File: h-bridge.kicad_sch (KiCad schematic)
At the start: 10 parts, among them U5 DRV8874, U6 INA241A3IDDF

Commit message: schem: add missing footprints
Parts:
- R3: footprint (none) -> Resistor_SMD:R_0805_2012Metric
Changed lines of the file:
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@@
 			)
 		)
-		(property "Footprint" ""
+		(property "Footprint" "Resistor_SMD:R_0805_2012Metric"
 			(at 168.91 90.678 90)
 			(hide yes)

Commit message: schem: add ordering info to BOM
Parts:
- R3: Basic (none) -> X; JLCPCB Part # (none) -> C22450688; Manufacturer (none) -> Milliohm; Manufacturer Part Number (none) -> HoYLR0805-1/2W-10mR-1%
- U5: Basic (none) -> X; JLCPCB Part # (none) -> C1855818; Manufacturer (none) -> Texas Instruments; Manufacturer Part Number (none) -> DRV8874PWPR
- U6: Basic (none) -> X; JLCPCB Part # (none) -> C6051860; Manufacturer (none) -> Texas Instruments; Manufacturer Part Number (none) -> INA241A3IDDFR

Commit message: schem: add title
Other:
- company: (none) -> Rémi Ait-Younes
- title: (none) -> Stepper FOC CAN 1
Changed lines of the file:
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@@
 	(generator_version "10.0")
 	(paper "A4")
+	(title_block
+		(title "Stepper FOC CAN 1")
+		(date "2026-04-11")
+		(rev "01")
+		(company "Rémi Ait-Younes")
+	)
 	(text "Gain: 50V/V\nRange: ±3.35A"
 		(exclude_from_sim no)

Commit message: schem: reannotate
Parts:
- renumbered C26 to C29, C25 to C30, R6 to R10, R3 to R11, TP5 to TP2, U5 to U6, U6 to U7
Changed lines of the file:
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@@
 		(in_pos_files yes)
 		(dnp no)
-		(property "Reference" "#PWR035"
+		(property "Reference" "#PWR049"
 			(at 129.54 119.38 0)
 			(hide yes)
@@
 			(project "stepper-foc-can-1"
 				(path "/7e511d2f-8abe-4907-a647-133ba6c8a8df/0e6f64a8-6e8e-4ac8-9891-7840f5dbe0f5"
-					(reference "#PWR035")
+					(reference "#PWR049")
 					(unit 1)
 				)
 				(path "/7e511d2f-8abe-4907-a647-133ba6c8a8df/8e42ab5e-b2ac-4617-9b8b-7bb81c6c35e1"
-					(reference "#PWR054")
+					(reference "#PWR059")
 					(unit 1)
 				)
@@
 		(in_pos_files yes)
 		(dnp no)
-		(property "Reference" "#PWR045"
+		(property "Reference" "#PWR048"
 			(at 129.54 83.82 0)
 			(hide yes)
@@
 			(project "stepper-foc-can-1"
 				(path "/7e511d2f-8abe-4907-a647-133ba6c8a8df/0e6f64a8-6e8e-4ac8-9891-7840f5dbe0f5"
-					(reference "#PWR045")
+					(reference "#PWR048")
 					(unit 1)
 				)
 				(path "/7e511d2f-8abe-4907-a647-133ba6c8a8df/8e42ab5e-b2ac-4617-9b8b-7bb81c6c35e1"
-					(reference "#PWR053")
+					(reference "#PWR058")
 					(unit 1)
 				)
@@
 		(in_pos_files yes)
 		(dnp no)
-		(property "Reference" "U6"
+		(property "Reference" "U7"
 			(at 161.798 96.266 90)
 			(show_name no)
@@
 			(project "stepper-foc-can-1"
 				(path "/7e511d2f-8abe-4907-a647-133ba6c8a8df/0e6f64a8-6e8e-4ac8-9891-7840f5dbe0f5"
-					(reference "U6")
+					(reference "U7")
 					(unit 1)
 				)
 				(path "/7e511d2f-8abe-4907-a647-133ba6c8a8df/8e42ab5e-b2ac-4617-9b8b-7bb81c6c35e1"
-					(reference "U8")
+					(reference "U9")
 					(unit 1)
 				)
@@
 				)
 				(path "/7e511d2f-8abe-4907-a647-133ba6c8a8df/8e42ab5e-b2ac-4617-9b8b-7bb81c6c35e1"
-					(reference "#PWR051")
+					(reference "#PWR056")
 					(unit 1)
 				)
@@
 		(in_pos_files yes)
 		(dnp no)
-		(property "Reference" "TP5"
+		(property "Reference" "TP2"
 			(at 167.386 115.062 0)
 			(show_name no)
@@
 			(project "stepper-foc-can-1"
 				(path "/7e511d2f-8abe-4907-a647-133ba6c8a8df/0e6f64a8-6e8e-4ac8-9891-7840f5dbe0f5"
-					(reference "TP5")
+					(reference "TP2")
 					(unit 1)
 				)
 				(path "/7e511d2f-8abe-4907-a647-133ba6c8a8df/8e42ab5e-b2ac-4617-9b8b-7bb81c6c35e1"
-					(reference "TP6")
+					(reference "TP3")
 					(unit 1)
 				)
@@
 		(in_pos_files yes)
 		(dnp no)
-		(property "Reference" "#PWR050"
+		(property "Reference" "#PWR052"
 			(at 156.21 111.76 0)
 			(hide yes)
@@
 			(project "stepper-foc-can-1"
 				(path "/7e511d2f-8abe-4907-a647-133ba6c8a8df/0e6f64a8-6e8e-4ac8-9891-7840f5dbe0f5"
-					(reference "#PWR050")
+					(reference "#PWR052")
 					(unit 1)
 				)
 				(path "/7e511d2f-8abe-4907-a647-133ba6c8a8df/8e42ab5e-b2ac-4617-9b8b-7bb81c6c35e1"
-					(reference "#PWR057")
+					(reference "#PWR062")
 					(unit 1)
 				)
@@
 		(in_pos_files yes)
 		(dnp no)
-		(property "Reference" "C26"
+		(property "Reference" "C29"
 			(at 150.876 66.04 0)
 			(show_name no)
@@
 			(project "stepper-foc-can-1"
 				(path "/7e511d2f-8abe-4907-a647-133ba6c8a8df/0e6f64a8-6e8e-4ac8-9891-7840f5dbe0f5"
-					(reference "C26")
+					(reference "C29")
 					(unit 1)
 				)
@@
 		(in_pos_files yes)
 		(dnp no)
-		(property "Reference" "C25"
+		(property "Reference" "C30"
 			(at 159.258 76.2 0)
 			(show_name no)
@@
 			(project "stepper-foc-can-1"
 				(path "/7e511d2f-8abe-4907-a647-133ba6c8a8df/0e6f64a8-6e8e-4ac8-9891-7840f5dbe0f5"
-					(reference "C25")
+					(reference "C30")
 					(unit 1)
 				)
@@
 		(in_pos_files yes)
 		(dnp no)
-		(property "Reference" "#PWR043"
+		(property "Reference" "#PWR053"
 			(at 157.48 73.66 0)
 			(hide yes)
@@
 			(project "stepper-foc-can-1"
 				(path "/7e511d2f-8abe-4907-a647-133ba6c8a8df/0e6f64a8-6e8e-4ac8-9891-7840f5dbe0f5"
-					(reference "#PWR043")
+					(reference "#PWR053")
 					(unit 1)
 				)
 				(path "/7e511d2f-8abe-4907-a647-133ba6c8a8df/8e42ab5e-b2ac-4617-9b8b-7bb81c6c35e1"
-					(reference "#PWR058")
+					(reference "#PWR063")
 					(unit 1)
 				)
@@
 		(in_pos_files yes)
 		(dnp no)
-		(property "Reference" "#PWR048"
+		(property "Reference" "#PWR054"
 			(at 177.8 102.87 0)
 			(hide yes)
@@
 			(project "stepper-foc-can-1"
 				(path "/7e511d2f-8abe-4907-a647-133ba6c8a8df/0e6f64a8-6e8e-4ac8-9891-7840f5dbe0f5"
-					(reference "#PWR048")
+					(reference "#PWR054")
 					(unit 1)
 				)
 				(path "/7e511d2f-8abe-4907-a647-133ba6c8a8df/8e42ab5e-b2ac-4617-9b8b-7bb81c6c35e1"
-					(reference "#PWR059")
+					(reference "#PWR064")
 					(unit 1)
 				)
@@
 		(in_pos_files yes)
 		(dnp no)
-		(property "Reference" "#PWR044"
+		(property "Reference" "#PWR047"
 			(at 115.57 114.3 0)
 			(hide yes)
@@
 			(project "stepper-foc-can-1"
 				(path "/7e511d2f-8abe-4907-a647-133ba6c8a8df/0e6f64a8-6e8e-4ac8-9891-7840f5dbe0f5"
-					(reference "#PWR044")
+					(reference "#PWR047")
 					(unit 1)
 				)
 				(path "/7e511d2f-8abe-4907-a647-133ba6c8a8df/8e42ab5e-b2ac-4617-9b8b-7bb81c6c35e1"
-					(reference "#PWR052")
+					(reference "#PWR057")
 					(unit 1)
 				)
@@
 		(in_pos_files yes)
 		(dnp no)
-		(property "Reference" "R6"
+		(property "Reference" "R10"
 			(at 103.124 90.17 0)
 			(show_name no)
@@
 			(project "stepper-foc-can-1"
 				(path "/7e511d2f-8abe-4907-a647-133ba6c8a8df/0e6f64a8-6e8e-4ac8-9891-7840f5dbe0f5"
-					(reference "R6")
+					(reference "R10")
 					(unit 1)
 				)
 				(path "/7e511d2f-8abe-4907-a647-133ba6c8a8df/8e42ab5e-b2ac-4617-9b8b-7bb81c6c35e1"
-					(reference "R7")
+					(reference "R12")
 					(unit 1)
 				)
@@
 		(in_pos_files yes)
 		(dnp no)
-		(property "Reference" "#PWR036"
+		(property "Reference" "#PWR050"
 			(at 149.86 88.9 0)
 			(hide yes)
@@
 			(project "stepper-foc-can-1"
 				(path "/7e511d2f-8abe-4907-a647-133ba6c8a8df/0e6f64a8-6e8e-4ac8-9891-7840f5dbe0f5"
-					(reference "#PWR036")
+					(reference "#PWR050")
 					(unit 1)
 				)
 				(path "/7e511d2f-8abe-4907-a647-133ba6c8a8df/8e42ab5e-b2ac-4617-9b8b-7bb81c6c35e1"
-					(reference "#PWR055")
+					(reference "#PWR060")
 					(unit 1)
 				)
@@
 		(in_pos_files yes)
 		(dnp no)
-		(property "Reference" "#PWR047"
+		(property "Reference" "#PWR051"
 			(at 156.21 107.95 0)
 			(hide yes)
@@
 			(project "stepper-foc-can-1"
 				(path "/7e511d2f-8abe-4907-a647-133ba6c8a8df/0e6f64a8-6e8e-4ac8-9891-7840f5dbe0f5"
-					(reference "#PWR047")
+					(reference "#PWR051")
 					(unit 1)
 				)
 				(path "/7e511d2f-8abe-4907-a647-133ba6c8a8df/8e42ab5e-b2ac-4617-9b8b-7bb81c6c35e1"
-					(reference "#PWR056")
+					(reference "#PWR061")
 					(unit 1)
 				)
@@
 		(in_pos_files yes)
 		(dnp no)
-		(property "Reference" "R3"
+		(property "Reference" "R11"
 			(at 168.91 84.074 90)
 			(show_name no)
@@
 			(project "stepper-foc-can-1"
 				(path "/7e511d2f-8abe-4907-a647-133ba6c8a8df/0e6f64a8-6e8e-4ac8-9891-7840f5dbe0f5"
-					(reference "R3")
+					(reference "R11")
 					(unit 1)
 				)
 				(path "/7e511d2f-8abe-4907-a647-133ba6c8a8df/8e42ab5e-b2ac-4617-9b8b-7bb81c6c35e1"
-					(reference "R12")
+					(reference "R13")
 					(unit 1)
 				)
@@
 		(in_pos_files yes)
 		(dnp no)
-		(property "Reference" "#PWR049"
+		(property "Reference" "#PWR055"
 			(at 177.8 116.84 0)
 			(hide yes)
@@
 			(project "stepper-foc-can-1"
 				(path "/7e511d2f-8abe-4907-a647-133ba6c8a8df/0e6f64a8-6e8e-4ac8-9891-7840f5dbe0f5"
-					(reference "#PWR049")
+					(reference "#PWR055")
 					(unit 1)
 				)
 				(path "/7e511d2f-8abe-4907-a647-133ba6c8a8df/8e42ab5e-b2ac-4617-9b8b-7bb81c6c35e1"
-					(reference "#PWR060")
+					(reference "#PWR065")
 					(unit 1)
 				)
@@
 		(in_pos_files yes)
 		(dnp no)
-		(property "Reference" "U5"
+		(property "Reference" "U6"
 			(at 131.064 111.252 0)
 			(show_name no)
@@
 			(project "stepper-foc-can-1"
 				(path "/7e511d2f-8abe-4907-a647-133ba6c8a8df/0e6f64a8-6e8e-4ac8-9891-7840f5dbe0f5"
-					(reference "U5")
+					(reference "U6")
 					(unit 1)
 				)
 				(path "/7e511d2f-8abe-4907-a647-133ba6c8a8df/8e42ab5e-b2ac-4617-9b8b-7bb81c6c35e1"
-					(reference "U7")
-					(unit 1)
-				)
+					(reference "U8")
+					(unit 1)
+				)

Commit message: schem: update 22n capacitor PN
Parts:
- C28: footprint Capacitor_SMD:C_0603_1608Metric -> Capacitor_SMD:C_0402_1005Metric; JLCPCB Part # C21122 -> C1532; Manufacturer Samsung Electro-Mechanics -> FH (Guangdong Fenghua Advanced Tech); Manufacturer Part Number CL10B223KB8NNNC -> 0402B223K500NT
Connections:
- net GND: now also U6.17 (EPAD)
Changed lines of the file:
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@@
 			)
 		)
-		(property "Footprint" "Capacitor_SMD:C_0603_1608Metric"
+		(property "Footprint" "Capacitor_SMD:C_0402_1005Metric"
 			(at 151.13 100.6348 0)
 			(hide yes)
@@
 			)
 		)
-		(property "JLCPCB Part #" "C21122"
+		(property "JLCPCB Part #" "C1532"
 			(at 147.32 101.6 90)
 			(hide yes)
@@
 			)
 		)
-		(property "Manufacturer" "Samsung Electro-Mechanics "
+		(property "Manufacturer" "FH (Guangdong Fenghua Advanced Tech)"
 			(at 147.32 101.6 90)
 			(hide yes)
@@
 			)
 		)
-		(property "Manufacturer Part Number" "CL10B223KB8NNNC"
-			(at 147.32 101.6 90)
-			(hide yes)
-			(show_name no)
-			(do_not_autoplace no)
-			(effects
-				(font
-					(size 1.27 1.27)
-				)
-			)
-		)
-		(property "KLC_S3.3" ""
-			(at 147.32 101.6 90)
-			(hide yes)
-			(show_name no)
-			(do_not_autoplace no)
-			(effects
-				(font
-					(size 1.27 1.27)
-				)
-			)
-		)
-		(property "KLC_S4.1" ""
+		(property "Manufacturer Part Number" "0402B223K500NT"
 			(at 147.32 101.6 90)
 			(hide yes)
@@
 		(pin "5"
 		)
+		(pin "17"
+		)
 		(instances

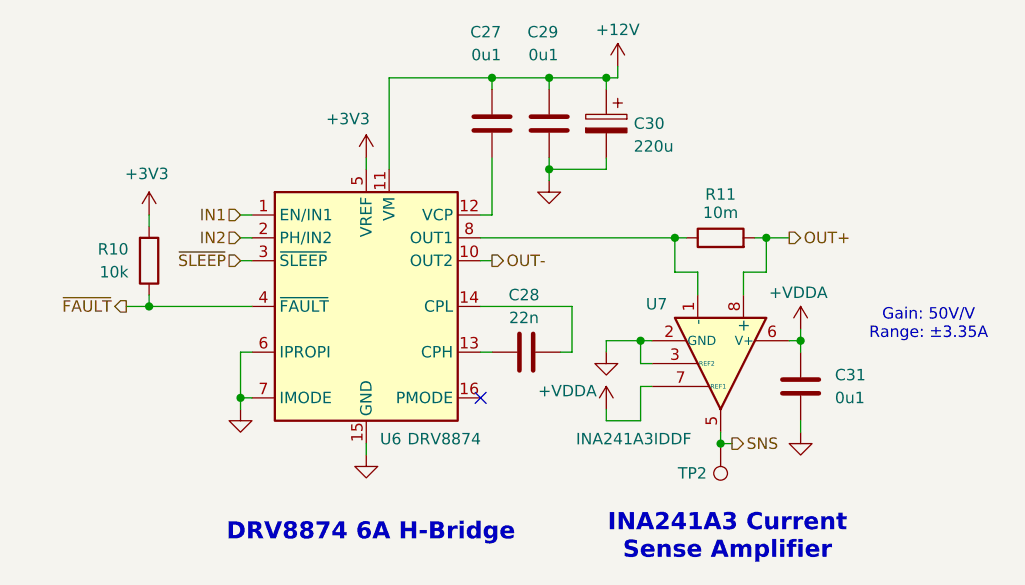
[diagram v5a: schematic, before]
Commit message: pcb: add drvs placement
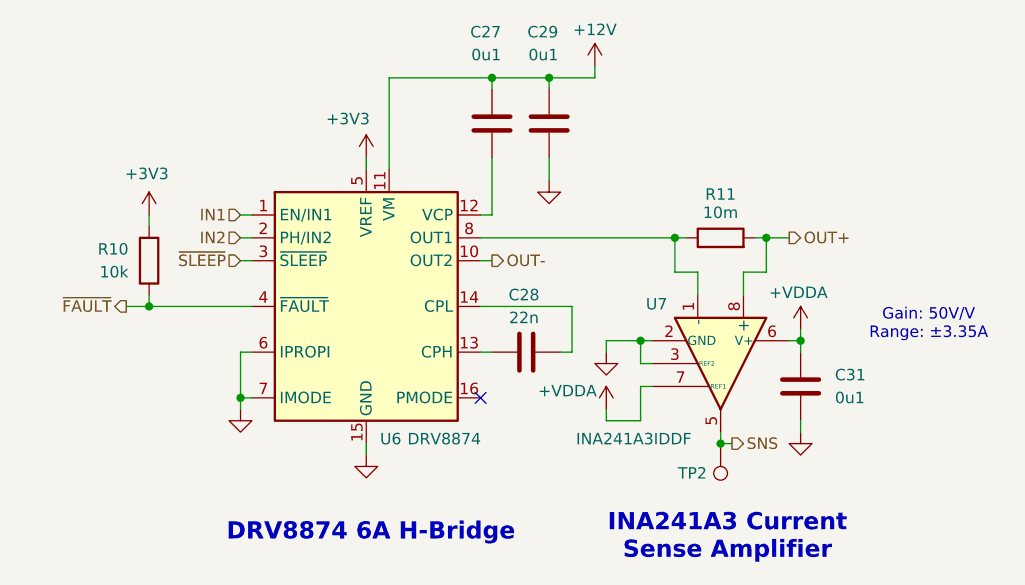
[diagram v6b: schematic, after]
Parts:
- removed C30: 220u, Capacitor_SMD:CP_Elec_6.3x7.7, symbol Device:C_Polarized
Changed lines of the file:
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@@
-	)
-	(junction
-		(at 156.21 71.12)
-		(diameter 0)
-		(color 0 0 0 0)
 	)
 	(junction
@@
 	)
 	(junction
-		(at 149.86 81.28)
-		(diameter 0)
-		(color 0 0 0 0)
-	)
-	(junction
 		(at 168.91 111.76)
 		(diameter 0)
@@
 	(wire
 		(pts
-			(xy 157.48 71.12) (xy 156.21 71.12)
+			(xy 149.86 71.12) (xy 154.94 71.12)
 		)
 		(stroke
@@
 	(wire
 		(pts
-			(xy 156.21 80.01) (xy 156.21 81.28)
-		)
-		(stroke
-			(width 0)
-			(type default)
-		)
-	)
-	(wire
-		(pts
 			(xy 129.54 80.01) (xy 129.54 81.28)
 		)
@@
 	(wire
 		(pts
-			(xy 157.48 69.85) (xy 157.48 71.12)
+			(xy 154.94 69.85) (xy 154.94 71.12)
 		)
 		(stroke
@@
 	(wire
 		(pts
-			(xy 156.21 71.12) (xy 156.21 72.39)
-		)
-		(stroke
-			(width 0)
-			(type default)
-		)
-	)
-	(wire
-		(pts
 			(xy 143.51 91.44) (xy 142.24 91.44)
 		)
@@
 	(wire
 		(pts
-			(xy 149.86 71.12) (xy 156.21 71.12)
-		)
-		(stroke
-			(width 0)
-			(type default)
-		)
-	)
-	(wire
-		(pts
-			(xy 149.86 80.01) (xy 149.86 81.28)
+			(xy 149.86 80.01) (xy 149.86 82.55)
 		)
 		(stroke
@@
 	(wire
 		(pts
-			(xy 156.21 81.28) (xy 149.86 81.28)
-		)
-		(stroke
-			(width 0)
-			(type default)
-		)
-	)
-	(wire
-		(pts
 			(xy 115.57 91.44) (xy 116.84 91.44)
 		)
@@
 		(pts
 			(xy 115.57 86.36) (xy 116.84 86.36)
-		)
-		(stroke
-			(width 0)
-			(type default)
-		)
-	)
-	(wire
-		(pts
-			(xy 149.86 81.28) (xy 149.86 82.55)
 		)
 		(stroke
@@
 	)
 	(symbol
-		(lib_id "Device:C_Polarized")
-		(at 156.21 76.2 0)
-		(mirror y)
-		(unit 1)
-		(body_style 1)
-		(exclude_from_sim no)
-		(in_bom yes)
-		(on_board yes)
-		(in_pos_files yes)
-		(dnp no)
-		(property "Reference" "C30"
-			(at 159.258 76.2 0)
-			(show_name no)
-			(do_not_autoplace no)
-			(effects
-				(font
-					(size 1.27 1.27)
-				)
-				(justify right)
-			)
-		)
-		(property "Value" "220u"
-			(at 159.258 78.74 0)
-			(show_name no)
-			(do_not_autoplace no)
-			(effects
-				(font
-					(size 1.27 1.27)
-				)
-				(justify right)
-			)
-		)
-		(property "Footprint" "Capacitor_SMD:CP_Elec_6.3x7.7"
-			(at 155.2448 80.01 0)
-			(hide yes)
-			(show_name no)
-			(do_not_autoplace no)
-			(effects
-				(font
-					(size 1.27 1.27)
-				)
-			)
-		)
-		(property "Datasheet" ""
-			(at 156.21 76.2 0)
-			(hide yes)
-			(show_name no)
-			(do_not_autoplace no)
-			(effects
-				(font
-					(size 1.27 1.27)
-				)
-			)
-		)
-		(property "Description" "Polarized capacitor"
-			(at 156.21 76.2 0)
-			(hide yes)
-			(show_name no)
-			(do_not_autoplace no)
-			(effects
-				(font
-					(size 1.27 1.27)
-				)
-			)
-		)
-		(property "Basic" "X"
-			(at 156.21 76.2 0)
-			(hide yes)
-			(show_name no)
-			(do_not_autoplace no)
-			(effects
-				(font
-					(size 1.27 1.27)
-				)
-			)
-		)
-		(property "JLCPCB Part #" "C2918361"
-			(at 156.21 76.2 0)
-			(hide yes)
-			(show_name no)
-			(do_not_autoplace no)
-			(effects
-				(font
-					(size 1.27 1.27)
-				)
-			)
-		)
-		(property "Manufacturer" "ROQANG"
-			(at 156.21 76.2 0)
-			(hide yes)
-			(show_name no)
-			(do_not_autoplace no)
-			(effects
-				(font
-					(size 1.27 1.27)
-				)
-			)
-		)
-		(property "Manufacturer Part Number" "RVT1E221M0607"
-			(at 156.21 76.2 0)
-			(hide yes)
-			(show_name no)
-			(do_not_autoplace no)
-			(effects
-				(font
-					(size 1.27 1.27)
-				)
-			)
-		)
-		(property "KLC_S3.3" ""
-			(at 156.21 76.2 0)
-			(hide yes)
-			(show_name no)
-			(do_not_autoplace no)
-			(effects
-				(font
-					(size 1.27 1.27)
-				)
-			)
-		)
-		(property "KLC_S4.1" ""
-			(at 156.21 76.2 0)
-			(hide yes)
-			(show_name no)
-			(do_not_autoplace no)
-			(effects
-				(font
-					(size 1.27 1.27)
-				)
-			)
-		)
-		(pin "2"
-		)
-		(pin "1"
-		)
-		(instances
-			(project "stepper-foc-can-1"
-				(path "/7e511d2f-8abe-4907-a647-133ba6c8a8df/0e6f64a8-6e8e-4ac8-9891-7840f5dbe0f5"
-					(reference "C30")
-					(unit 1)
-				)
-				(path "/7e511d2f-8abe-4907-a647-133ba6c8a8df/8e42ab5e-b2ac-4617-9b8b-7bb81c6c35e1"
-					(reference "C35")
-					(unit 1)
-				)
-			)
-		)
-	)
-	(symbol
 		(lib_id "Device:C")
 		(at 147.32 101.6 90)
@@
 	(symbol
 		(lib_id "power:+12V")
-		(at 157.48 69.85 0)
+		(at 154.94 69.85 0)
 		(unit 1)
 		(body_style 1)
@@
 		(dnp no)
 		(property "Reference" "#PWR053"
-			(at 157.48 73.66 0)
+			(at 154.94 73.66 0)
 			(hide yes)
 			(show_name no)
@@
 		)
 		(property "Value" "+12V"
-			(at 157.48 65.786 0)
+			(at 154.94 65.786 0)
 			(show_name no)
 			(do_not_autoplace no)
@@
 		)
 		(property "Footprint" ""
-			(at 157.48 69.85 0)
+			(at 154.94 69.85 0)
 			(hide yes)
 			(show_name no)
@@
 		)
 		(property "Datasheet" ""
-			(at 157.48 69.85 0)
+			(at 154.94 69.85 0)
 			(hide yes)
 			(show_name no)
@@
 		)
 		(property "Description" "Power symbol creates a global label with name \"+12V\""
-			(at 157.48 69.85 0)
-			(hide yes)
-			(show_name no)
+			(at 154.94 69.85 0)
+			(hide yes)
+			(show_name no)
